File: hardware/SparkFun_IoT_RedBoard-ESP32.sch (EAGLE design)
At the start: 120 parts, among them J1 5.5x2.1mm Barrel, J13 QWIIC_RIGHT_ANGLE, J15 MICRO-SD-PUSH-PUSH-EXT-PIN, J2 USB-C, J3 USB_SOLDER_PADS, J5 M10NO_SILK, Q1 MBT3904DW1T1, Q11 20V/4.2A/52mΩ/1.4W, Q13 20V/4.2A/52mΩ/1.4W, Q3 20V/4.2A/52mΩ/1.4W, Q5 20V/4.2A/52mΩ/1.4W, Q7 20V/4.2A/52mΩ/1.4W, Q9 20V/4.2A/52mΩ/1.4W, U1 ESP-WROOM-3232D, U2 CH340C, U3 LM1117, U4 3.3V, U5 MCP73831, U6 MAX17048

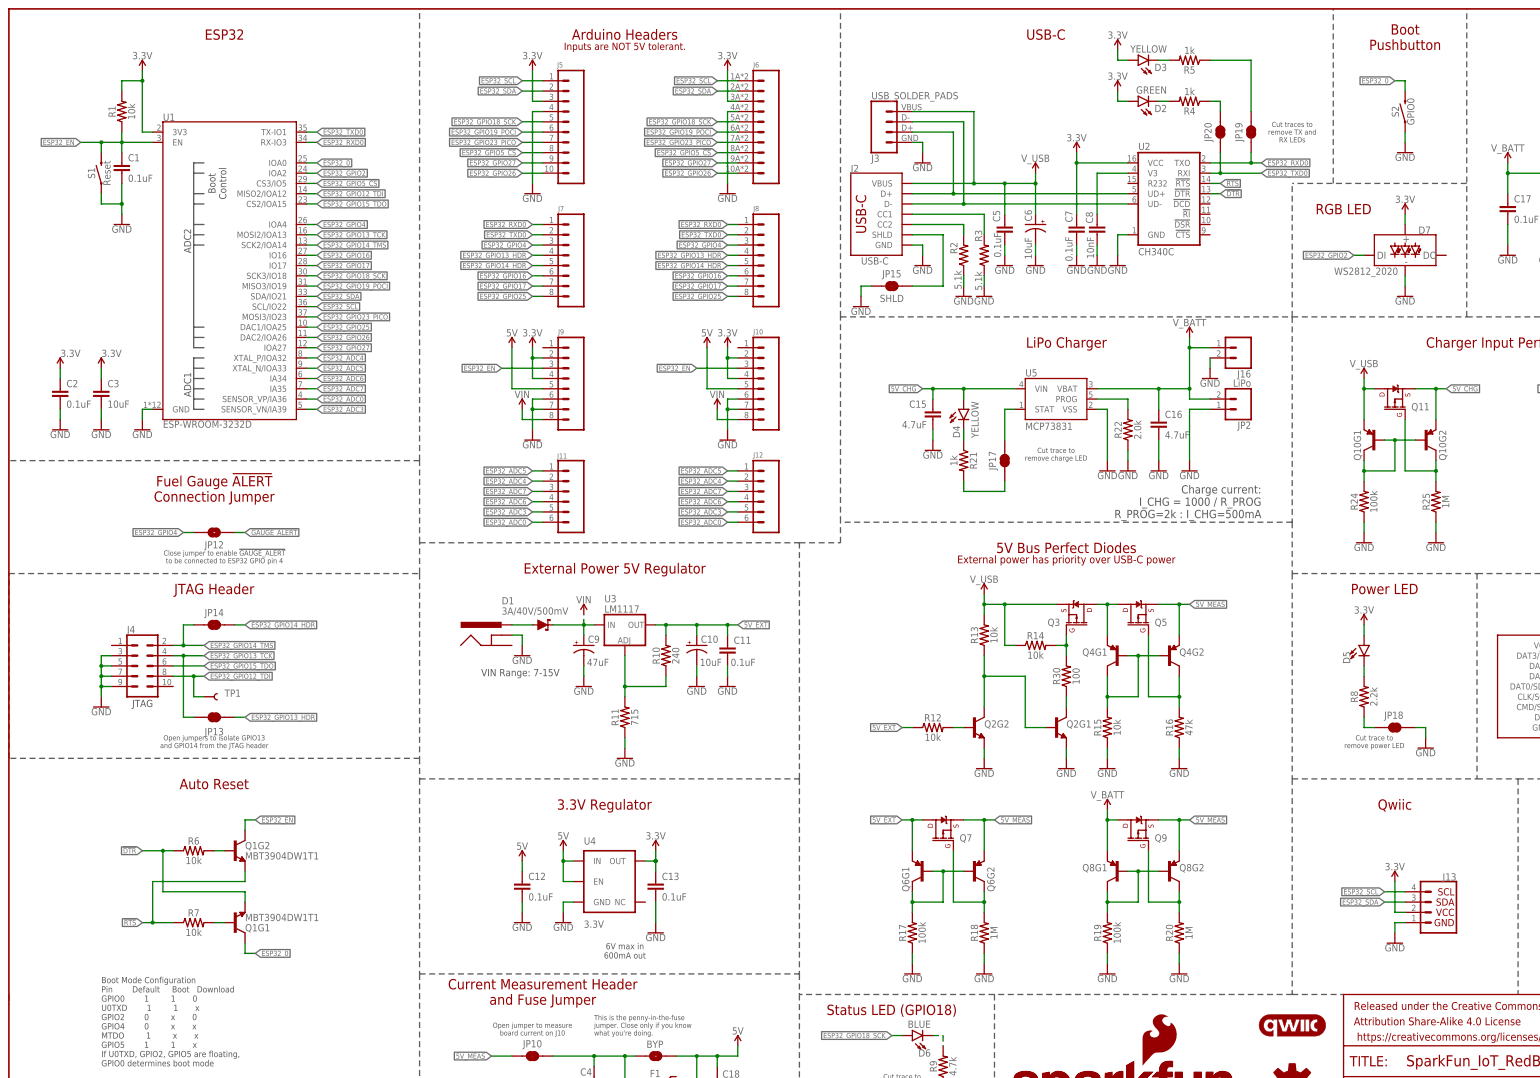
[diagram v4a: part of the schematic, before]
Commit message: Design review updates
Add decoupling cap for WS2812
Move SparkFun logo in top silk
Add GND via for 3V regulator
Change I2C label to use superscript 2
Remove extraneous lines in schematic
Add warnings about ESP32 boot pins and ADC2/WiFi to schematic
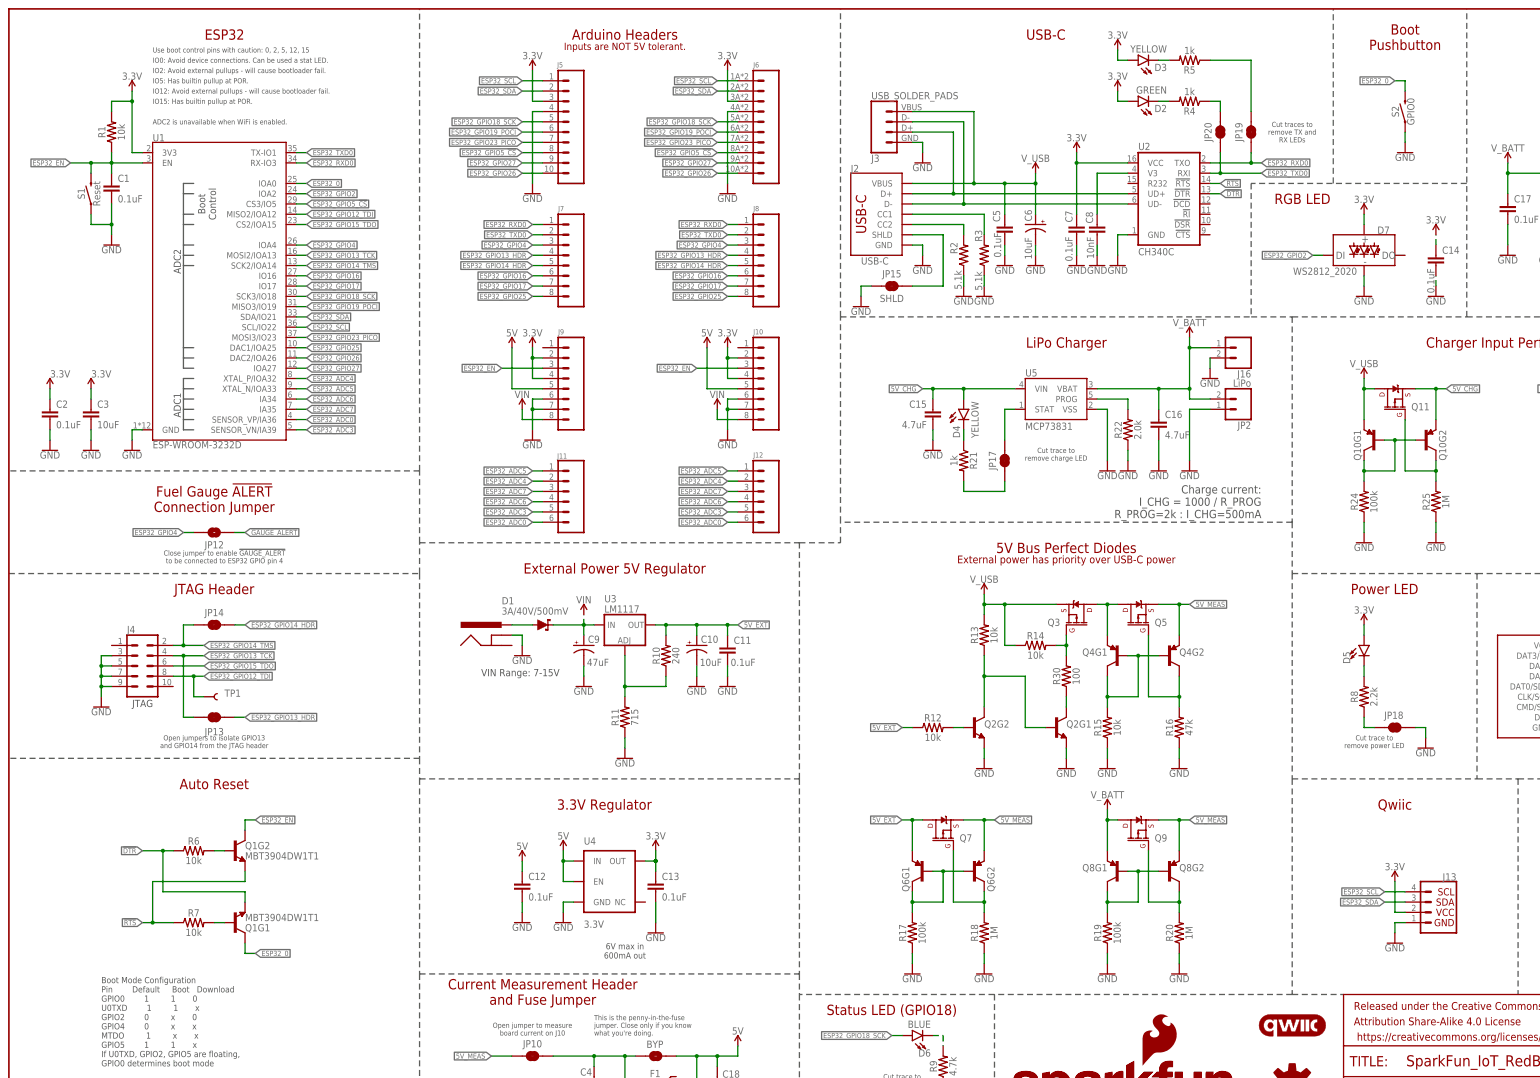
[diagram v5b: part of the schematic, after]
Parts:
- added C14: 0.1uF, SparkFun-Capacitors:0.1UF-0603-25V-(+80/-20%)
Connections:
- net 3.3V: now also C14.1
- net GND: now also C14.2
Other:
- note added: "ADC2 is unavailable when WiFi is enabled."
- note added: "IO0: Avoid device connections. Can be used a stat LED."
- note added: "IO12: Avoid external pullups - will cause bootloader fail."
- note added: "IO15: Has builtin pullup at POR."
- note added: "IO2: Avoid external pullups - will cause bootloader fail."
- note added: "IO5: Has builtin pullup at POR."
- note added: "Use boot control pins with caution: 0, 2, 5, 12, 15"
- moved on the sheet: C1, C2, C3, D7, R1, S1, U1

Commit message: Design Review Updates
Change "Revised by" to vector font in tDocu
Rename jumpers based on their functions
Add GND trace between GPIO 16/17 in layer 3
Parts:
- renumbered JP10 to MEAS, JP11 to I2C, JP12 to !ALERT!, JP13 to TCK, JP14 to TMS, JP15 to SHLD, JP16 to SD_DET, JP17 to LED_CHG, JP18 to LED_PWR, JP19 to LED_RX, JP20 to LED_TX, JP21 to LED_18
